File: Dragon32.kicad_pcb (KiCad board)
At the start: 2 copper layers, 253 x 169.1 mm, 184 parts, among them IC1 LM393DR, IC10 74ACT138, IC11 74ACT244N, IC16 74ACT244N, IC19 MC6809E, IC24 74ACT244N, IC31 74ACT02, IC33 74ACT138N, IC34 CD4050BDR, J1 Video Output Female, J2 Board Interconnect Female, J3 Conn_02x08_Odd_Even, J4 JTAG, J5 6-bit DAC, J6 Audio Left, J7 Audio Right, J8 Stereo, SW1 RESET, U1 AS6C1008-TIN, U10 4052, U11 TS5A3166DBVR, U12 6551, U13 4069, U14 LM348DR, U17 74LS08, U2 AS6C1008-55TIN, U3 XC95144XL-TQ100, U4 TPS7A2433DBVR, U5 W65C21, U6 W65C21, U7 W65C21, U8 28C256, U9 74HCT1G08, X1 14.31818MHz, X2 1.8432MHz

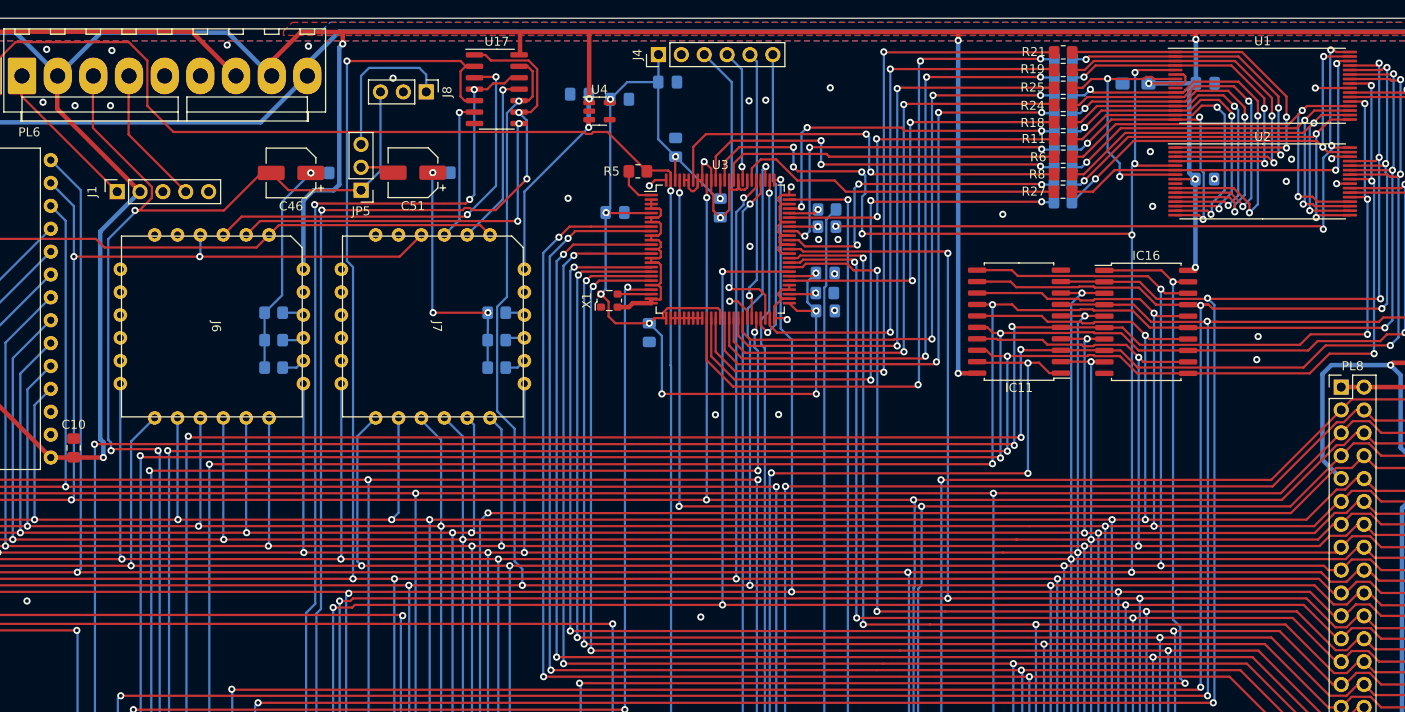
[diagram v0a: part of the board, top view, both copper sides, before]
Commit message: fix OE timing on SRAM
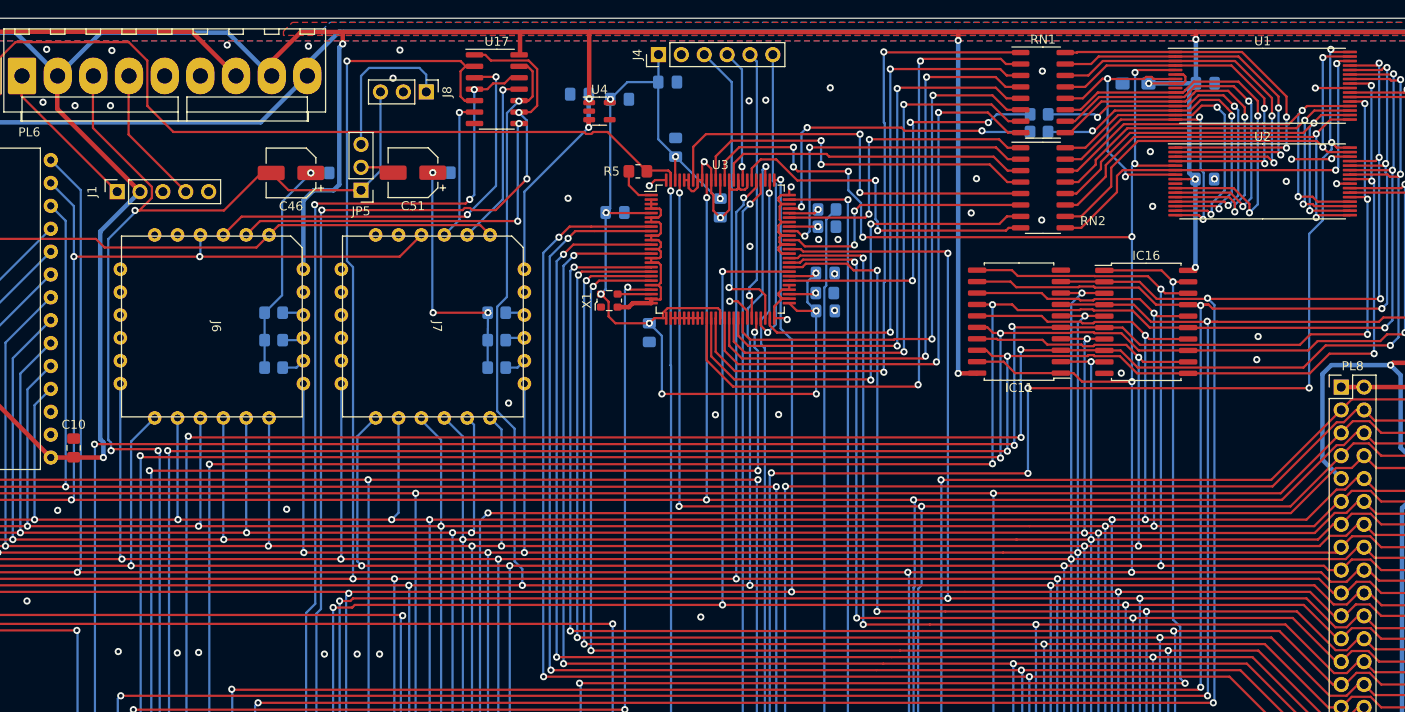
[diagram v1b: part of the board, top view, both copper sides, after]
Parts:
- removed R10, R11, R12, R17, R18, R19, R21, R22, R23, R24, R25, R26, R6, R7, R8, R9: 22R, Resistor_SMD:R_0805_2012Metric_Pad1.20x1.40mm_HandSolder
- added RN1: 22R, Package_SO:SOIC-16_3.9x9.9mm_P1.27mm, F.Cu at (262.5, 40.0)
- added RN2: 22R, Package_SO:SOIC-16_3.9x9.9mm_P1.27mm, F.Cu at (262.5, 50.5)
- R27: moved to B.Cu
- moved R27 8.98 mm to (262.1, 42.4)
- moved R20 8.24 mm to (262.1, 44.3)
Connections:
- IC11 pad 1: Net-(IC11-OEa) -> R/~{W}
- IC11 pad 19: Net-(IC11-OEa) -> R/~{W}
- IC31 pad 4: Net-(IC11-OEa) -> ~{R}/W
- R20 pad 1: Z10 -> Z6
- R20 pad 2: Net-(U3-P36) -> Net-(U3-P72)
- R27 pad 1: Z17 -> Z7
- R27 pad 2: Net-(U3-P81) -> Net-(U3-P56)
- U1 pad 32: ~{CAS} -> ~{R}/W
- U2 pad 32: ~{CAS} -> ~{R}/W
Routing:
- net ~{R}/W: track 0.00 -> 292.8 mm, vias 0 -> 9
- net Net-(IC11-OEa): track 231.0 -> 0.00 mm, vias 6 -> 0
- net ~{CAS}: track 79.2 -> 0.00 mm, vias 4 -> 0
- net R/~{W}: track 592.6 -> 610.0 mm, vias 15 -> 16
- net Net-(U3-P65): track 36.9 -> 30.3 mm, vias 3 -> 2
- net Net-(U3-P36): track 63.4 -> 57.4 mm, vias 3 -> 2
- net GND: track 96.7 -> 101.1 mm, vias 123 -> 137
- net Net-(U3-P70): track 38.3 -> 34.6 mm
- net Net-(U3-P37): track 77.8 -> 74.1 mm
- net Net-(U3-P35): track 80.7 -> 77.2 mm, vias 3 -> 2
- net Z17: track 43.9 -> 47.3 mm
- net Net-(U3-P49): track 62.0 -> 58.5 mm
- net Net-(U3-P67): track 39.3 -> 36.0 mm, vias 3 -> 2
- net Net-(U3-P40): track 70.8 -> 67.5 mm, vias 3 -> 2
- net Net-(U3-P42): track 66.1 -> 62.9 mm
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
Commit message: update page info
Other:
- board text added: "Proto 2"
- board text added: "REVISION X4"
- board text added: "Revision x4.0"
- board text added: "SAMx4 by Ciaran Anscomb"
- board text removed: "Proto 1"
- board text removed: "REVISION 3"
- board text removed: "Revision 3.0"

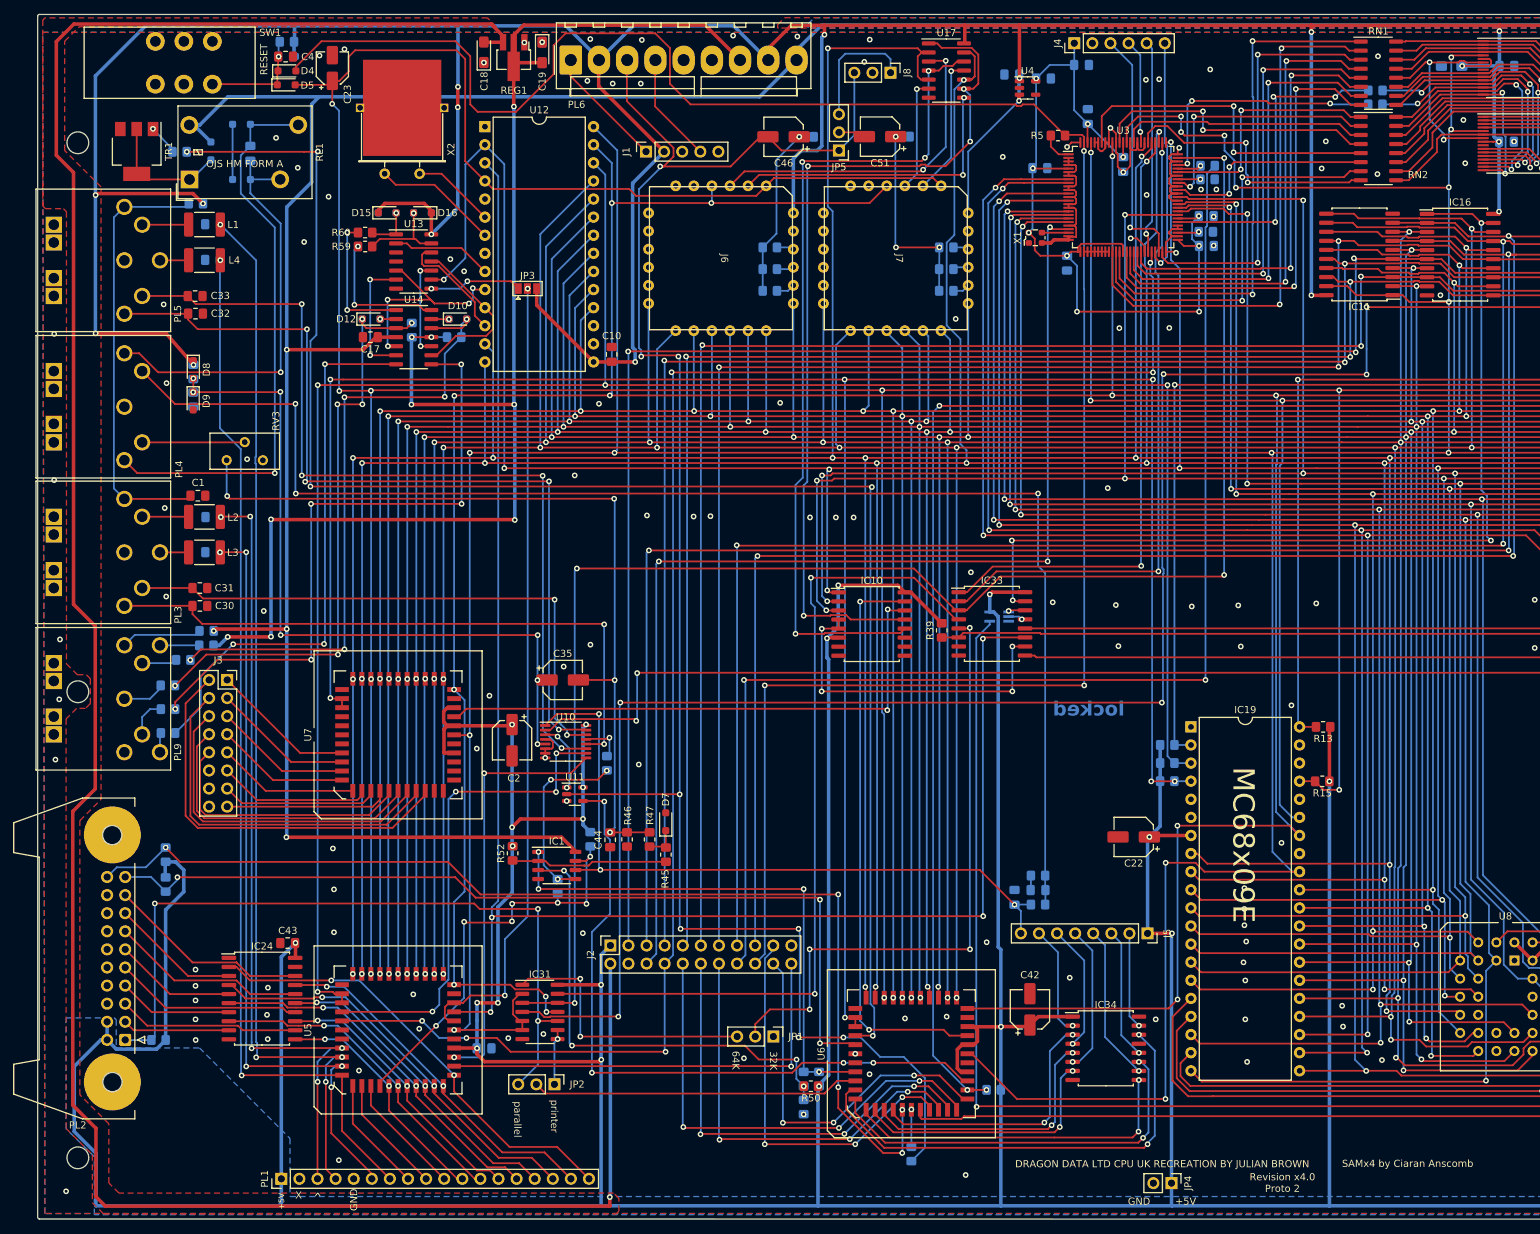
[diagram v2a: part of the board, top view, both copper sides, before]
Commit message: move -5v
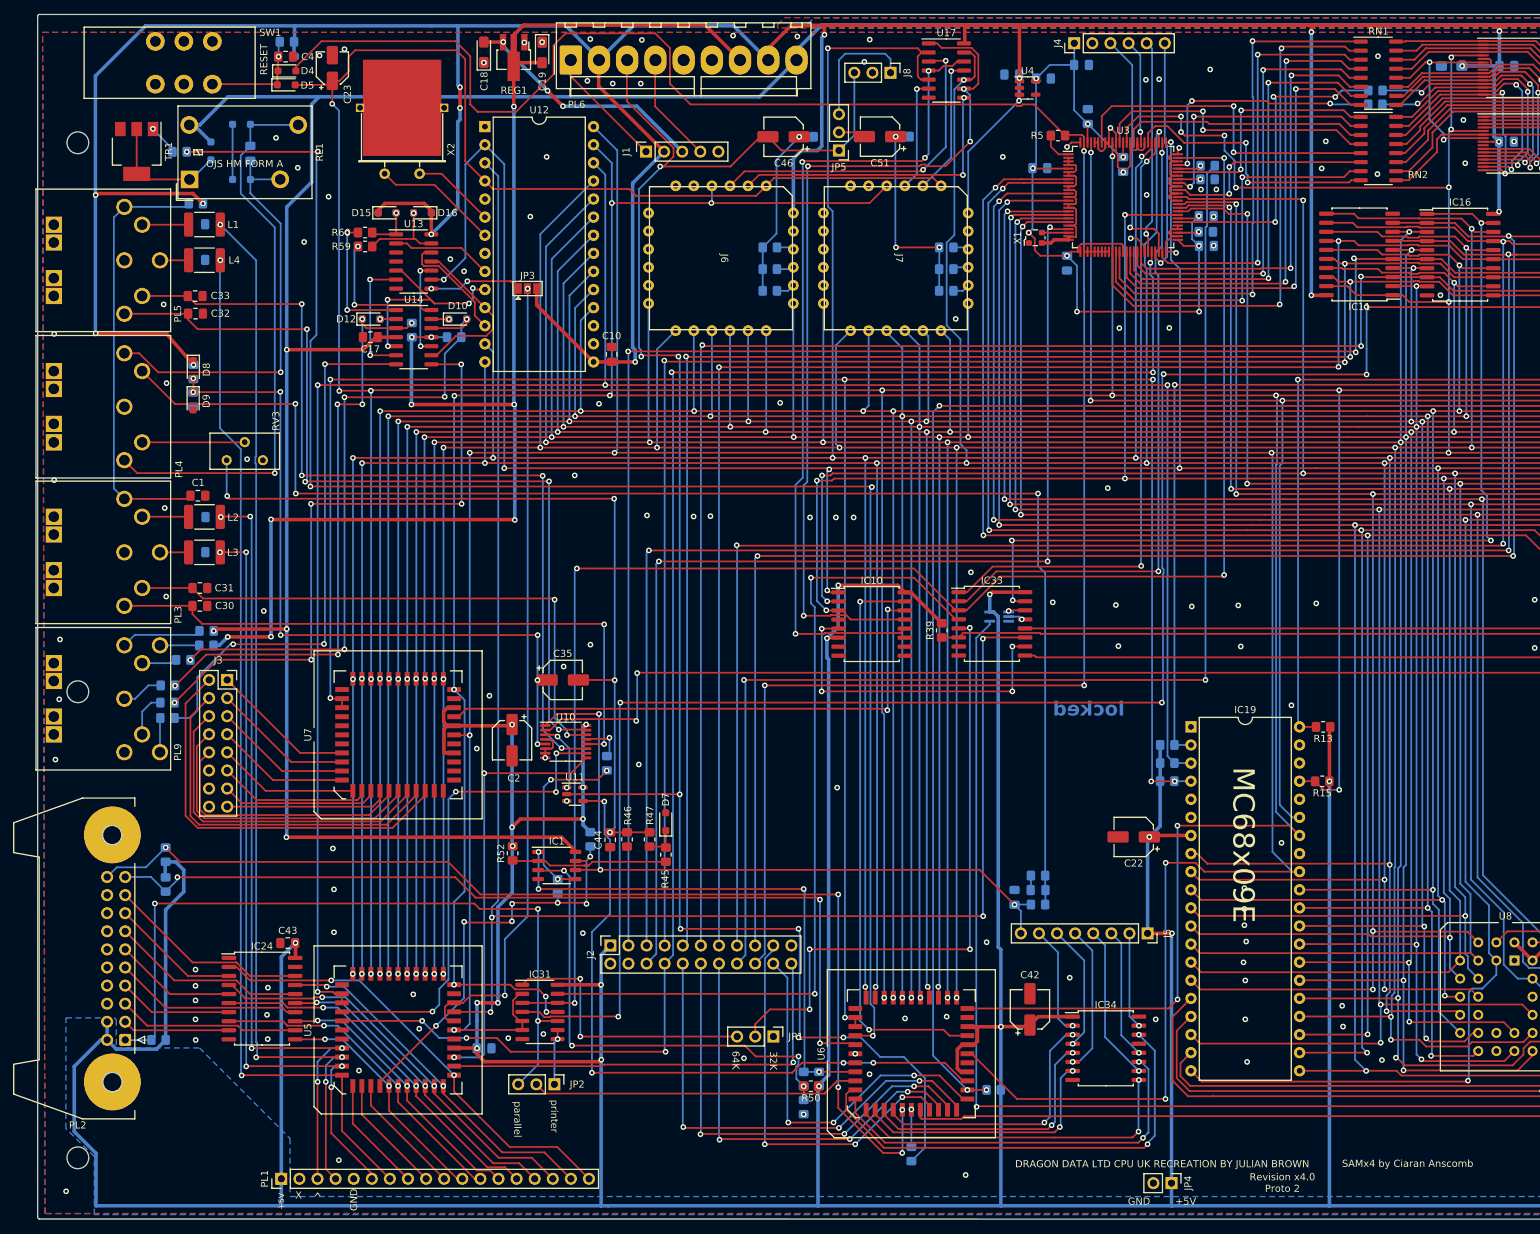
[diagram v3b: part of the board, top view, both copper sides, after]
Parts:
- moved R37 2.11 mm to (92.6, 130.4)
- moved R35 0.92 mm to (92.6, 128.3)
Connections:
- J1 pad 3: unconnected-(J1-Pin_3-Pad3) -> -5V
- J2 pad 2: -5V -> unconnected-(J2-Pin_2-Pad2)
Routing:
- net -5V: track 341.7 -> 34.6 mm, vias 1 -> 3
- net Net-(PL9-Pad6): track 2.75 -> 4.83 mm
- net Net-(U14C-OUT): track 89.3 -> 88.5 mm
- net Net-(PL9-Pad4): track 5.52 -> 6.27 mm
- net A12: track 279.9 -> 279.2 mm
- net Net-(IC1A-+): track 67.0 -> 67.6 mm
- net Net-(U14B-OUT): track 77.9 -> 77.3 mm
- net GND: vias 137 -> 140
- removed copper zone on F.Cu, net -5V
